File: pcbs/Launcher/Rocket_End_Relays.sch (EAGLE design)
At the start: 40 parts, among them IC2 LM2576T-ADJ, K4 LD105, K5 LD105, K6 LD105, K7 LD105, T1 BC547, T2 BC547, T3 BC547, T4 BC547, T5 BC547, U1 ARDUINO-MEGAPRO-5V, X1 1751248, X2 22-23-2041, X3 22-23-2021, X4 1751248, X5 22-23-2021

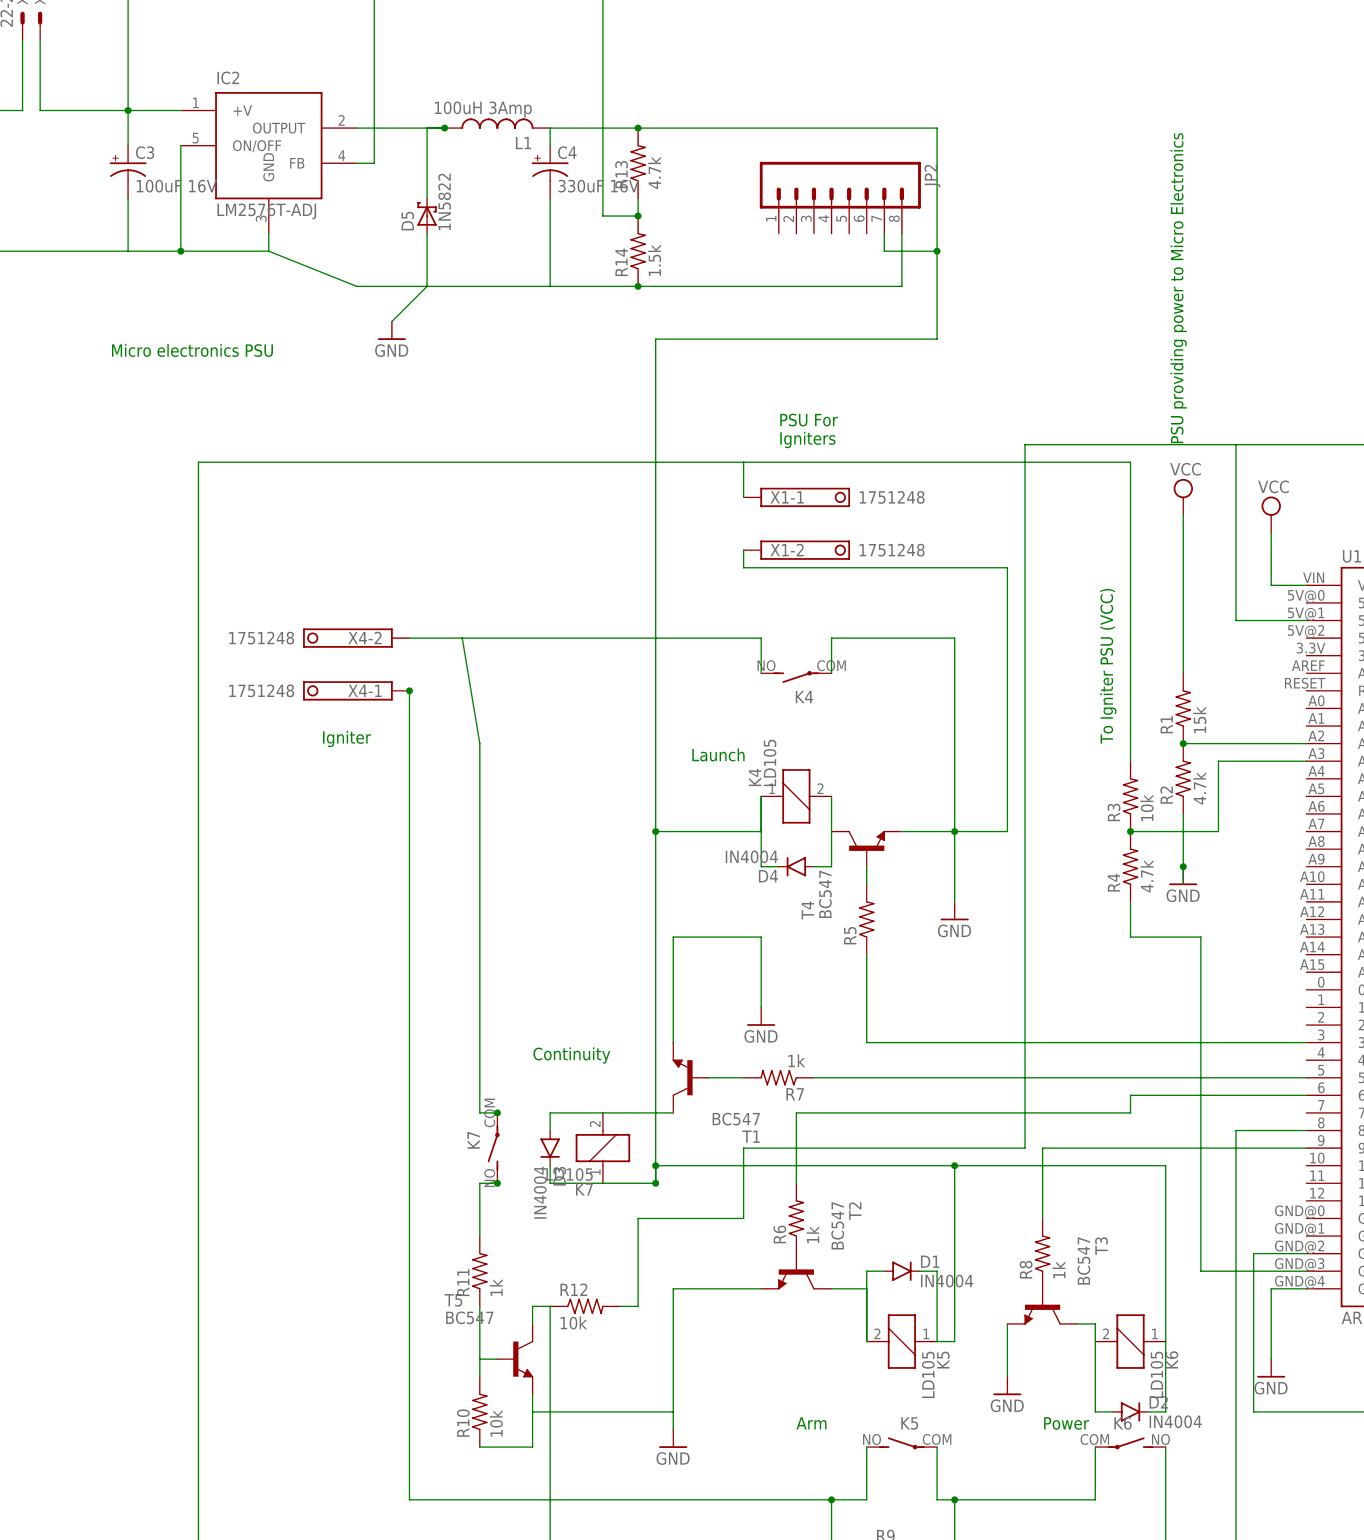
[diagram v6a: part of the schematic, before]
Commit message: * More refinements to tracks, making sure the gaps are sufficiently large.
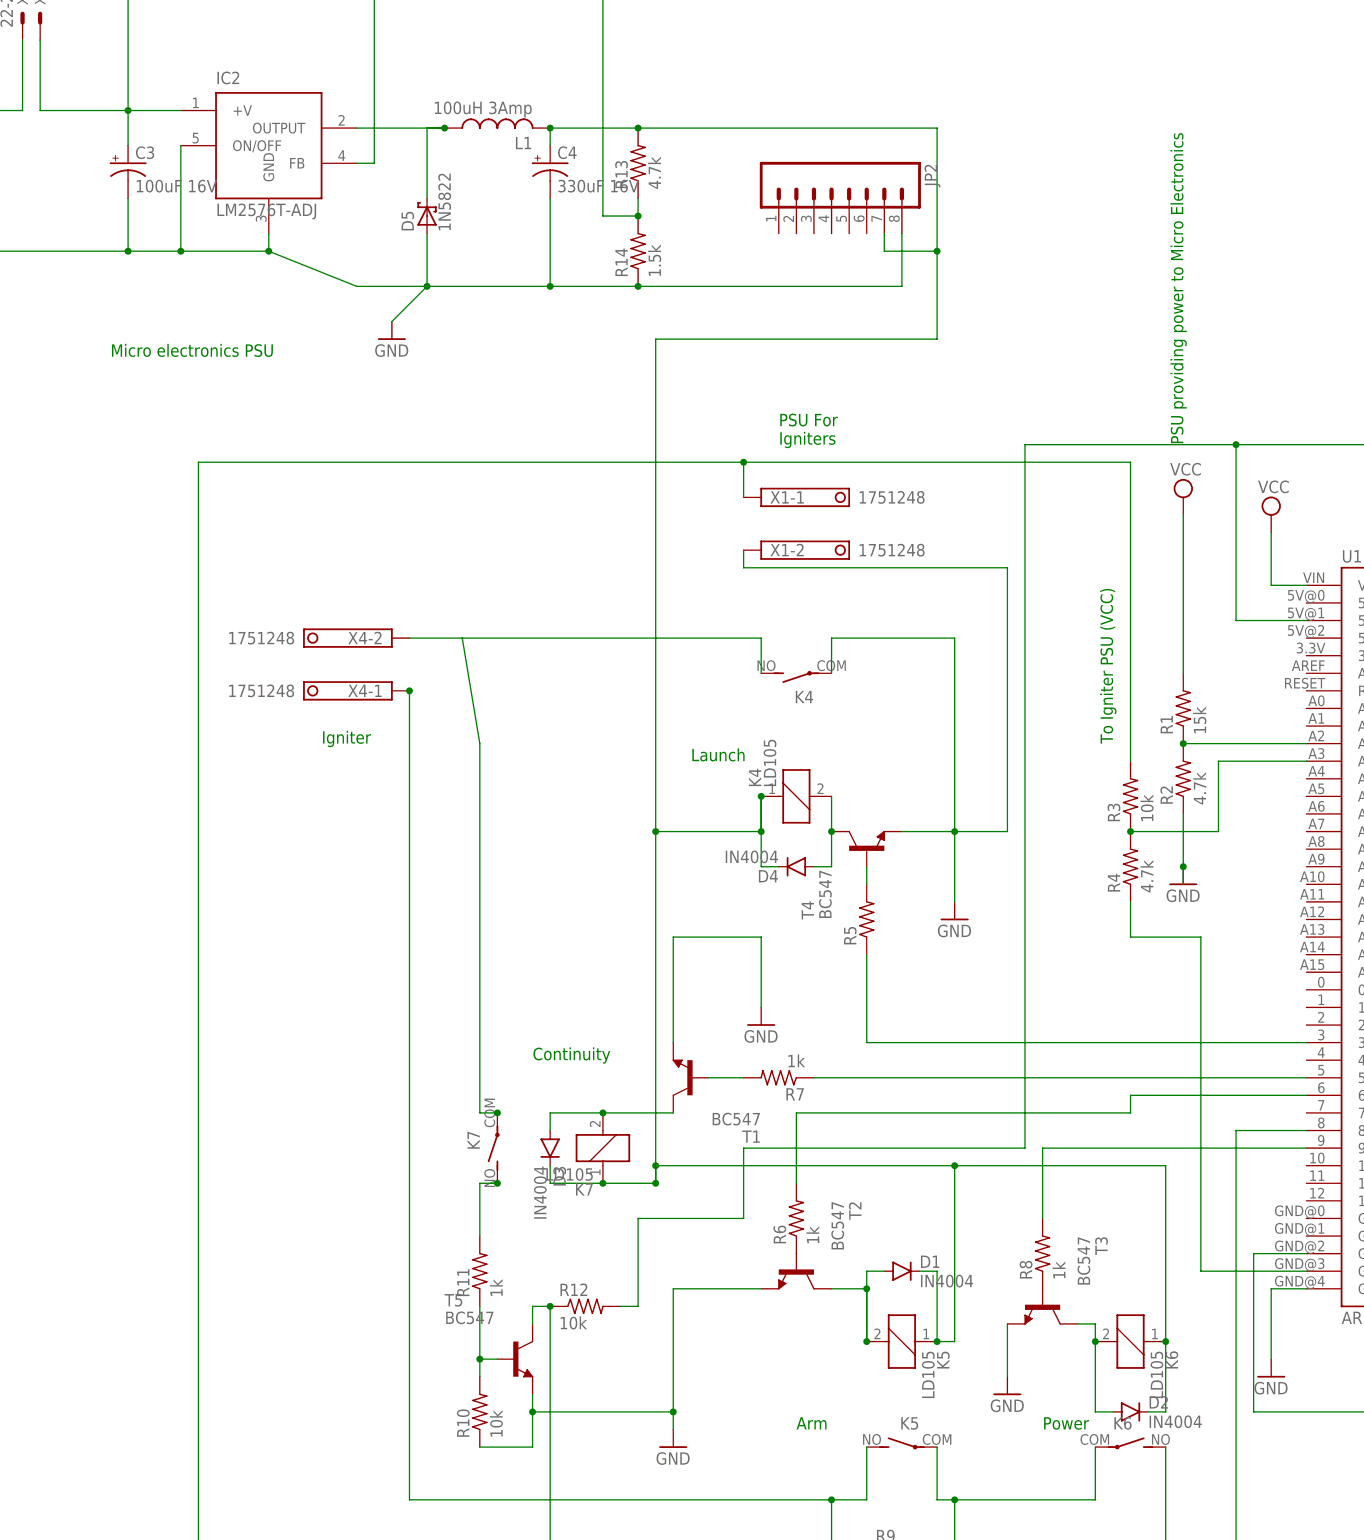
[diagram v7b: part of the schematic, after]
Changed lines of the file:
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@@
 <wire x1="-99.06" y1="-20.32" x2="-91.44" y2="-20.32" width="0.1524" layer="91"/>
 <wire x1="-91.44" y1="-20.32" x2="-91.44" y2="-15.24" width="0.1524" layer="91"/>
+<junction x="-91.44" y="-15.24"/>
+<junction x="-71.12" y="-15.24"/>
 </segment>
 <segment>
@@
 <pinref part="JP2" gate="G$1" pin="8"/>
 <wire x1="-38.1" y1="147.32" x2="-38.1" y2="154.94" width="0.1524" layer="91"/>
+<junction x="-88.9" y="147.32"/>
+<junction x="-149.86" y="152.4"/>
+<junction x="-106.68" y="147.32"/>
+<junction x="-129.54" y="152.4"/>
 </segment>
 </net>
@@
 <wire x1="-50.8" y1="63.5" x2="-48.26" y2="63.5" width="0.1524" layer="91"/>
 <wire x1="-48.26" y1="63.5" x2="-48.26" y2="68.58" width="0.1524" layer="91"/>
+<junction x="-48.26" y="68.58"/>
 </segment>
 </net>
@@
 <wire x1="-88.9" y1="25.4" x2="-88.9" y2="27.94" width="0.1524" layer="91"/>
 <wire x1="-81.28" y1="27.94" x2="-88.9" y2="27.94" width="0.1524" layer="91"/>
+<junction x="-81.28" y="27.94"/>
 </segment>
 </net>
@@
 <wire x1="-7.62" y1="-15.24" x2="-10.16" y2="-15.24" width="0.1524" layer="91"/>
 <wire x1="-10.16" y1="-15.24" x2="-10.16" y2="-5.08" width="0.1524" layer="91"/>
+<junction x="-10.16" y="-5.08"/>
 </segment>
 </net>
@@
 <wire x1="-43.18" y1="2.54" x2="-43.18" y2="-5.08" width="0.1524" layer="91"/>
 <pinref part="K5" gate="1" pin="2"/>
-<wire x1="-43.18" y1="-5.08" x2="-43.18" y2="5.08" width="0.1524" layer="91"/>
+<wire x1="-43.18" y1="-5.08" x2="-43.18" y2="2.54" width="0.1524" layer="91"/>
 <pinref part="D1" gate="G$1" pin="A"/>
+<wire x1="-43.18" y1="2.54" x2="-43.18" y2="5.08" width="0.1524" layer="91"/>
 <wire x1="-43.18" y1="5.08" x2="-40.64" y2="5.08" width="0.1524" layer="91"/>
+<junction x="-43.18" y="2.54"/>
+<junction x="-43.18" y="-5.08"/>
 </segment>
 </net>
@@
 <wire x1="10.16" y1="-43.18" x2="-88.9" y2="-43.18" width="0.1524" layer="91"/>
 <wire x1="-88.9" y1="-43.18" x2="-88.9" y2="0" width="0.1524" layer="91"/>
+<junction x="-88.9" y="0"/>
 </segment>
 </net>
@@
 <wire x1="-99.06" y1="-7.62" x2="-99.06" y2="-10.16" width="0.1524" layer="91"/>
 <pinref part="R10" gate="G$1" pin="2"/>
+<junction x="-99.06" y="-7.62"/>
 </segment>
 </net>
@@
 <pinref part="K6" gate="2" pin="S"/>
 <pinref part="X1" gate="-1" pin="K"/>
+<junction x="-60.96" y="121.92"/>
 </segment>
 </net>
@@
 <pinref part="D4" gate="G$1" pin="C"/>
 <wire x1="-55.88" y1="63.5" x2="-58.42" y2="63.5" width="0.1524" layer="91"/>
-<wire x1="-58.42" y1="63.5" x2="-58.42" y2="73.66" width="0.1524" layer="91"/>
+<wire x1="-58.42" y1="63.5" x2="-58.42" y2="68.58" width="0.1524" layer="91"/>
+<wire x1="-58.42" y1="68.58" x2="-58.42" y2="73.66" width="0.1524" layer="91"/>
 <wire x1="0" y1="-5.08" x2="0" y2="-15.24" width="0.1524" layer="91"/>
 <pinref part="D2" gate="G$1" pin="C"/>
@@
 <wire x1="-40.64" y1="152.4" x2="-40.64" y2="154.94" width="0.1524" layer="91"/>
 <junction x="-33.02" y="152.4"/>
+<junction x="-58.42" y="68.58"/>
+<junction x="-81.28" y="17.78"/>
+<junction x="0" y="-5.08"/>
+<junction x="-33.02" y="-5.08"/>
+<junction x="-88.9" y="170.18"/>
+<junction x="-58.42" y="73.66"/>
 </segment>
 </net>
@@
 <wire x1="20.32" y1="99.06" x2="10.16" y2="99.06" width="0.1524" layer="91"/>
 <wire x1="-20.32" y1="124.46" x2="10.16" y2="124.46" width="0.1524" layer="91"/>
-</segment>
-</net>
+<junction x="10.16" y="124.46"/>
+</segment>
+</net>

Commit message: * Shortening names on various text fields...abbreviating them. * Added +/- to the igniter PSU connection.
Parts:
- R13: device resistor:R-US_0207/7 -> rcl:R-US_0204/5
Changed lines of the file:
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@@
 <part name="C4" library="rcl" deviceset="CPOL-US" device="E2-4" value="330uF 16V"/>
 <part name="L1" library="resistor" deviceset="L-US" device="TJ4-U1" value="100uH 3Amp"/>
-<part name="R13" library="resistor" deviceset="R-US_" device="0207/7" value="4.7k"/>
+<part name="R13" library="rcl" deviceset="R-US_" device="0204/5" value="4.7k"/>
 <part name="R14" library="resistor" deviceset="R-US_" device="0207/7" value="1.5k"/>
 <part name="D5" library="diode" deviceset="1N5908" device="" value="1N5822"/>
